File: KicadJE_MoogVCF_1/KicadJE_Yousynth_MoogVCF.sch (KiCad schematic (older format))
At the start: 44 parts

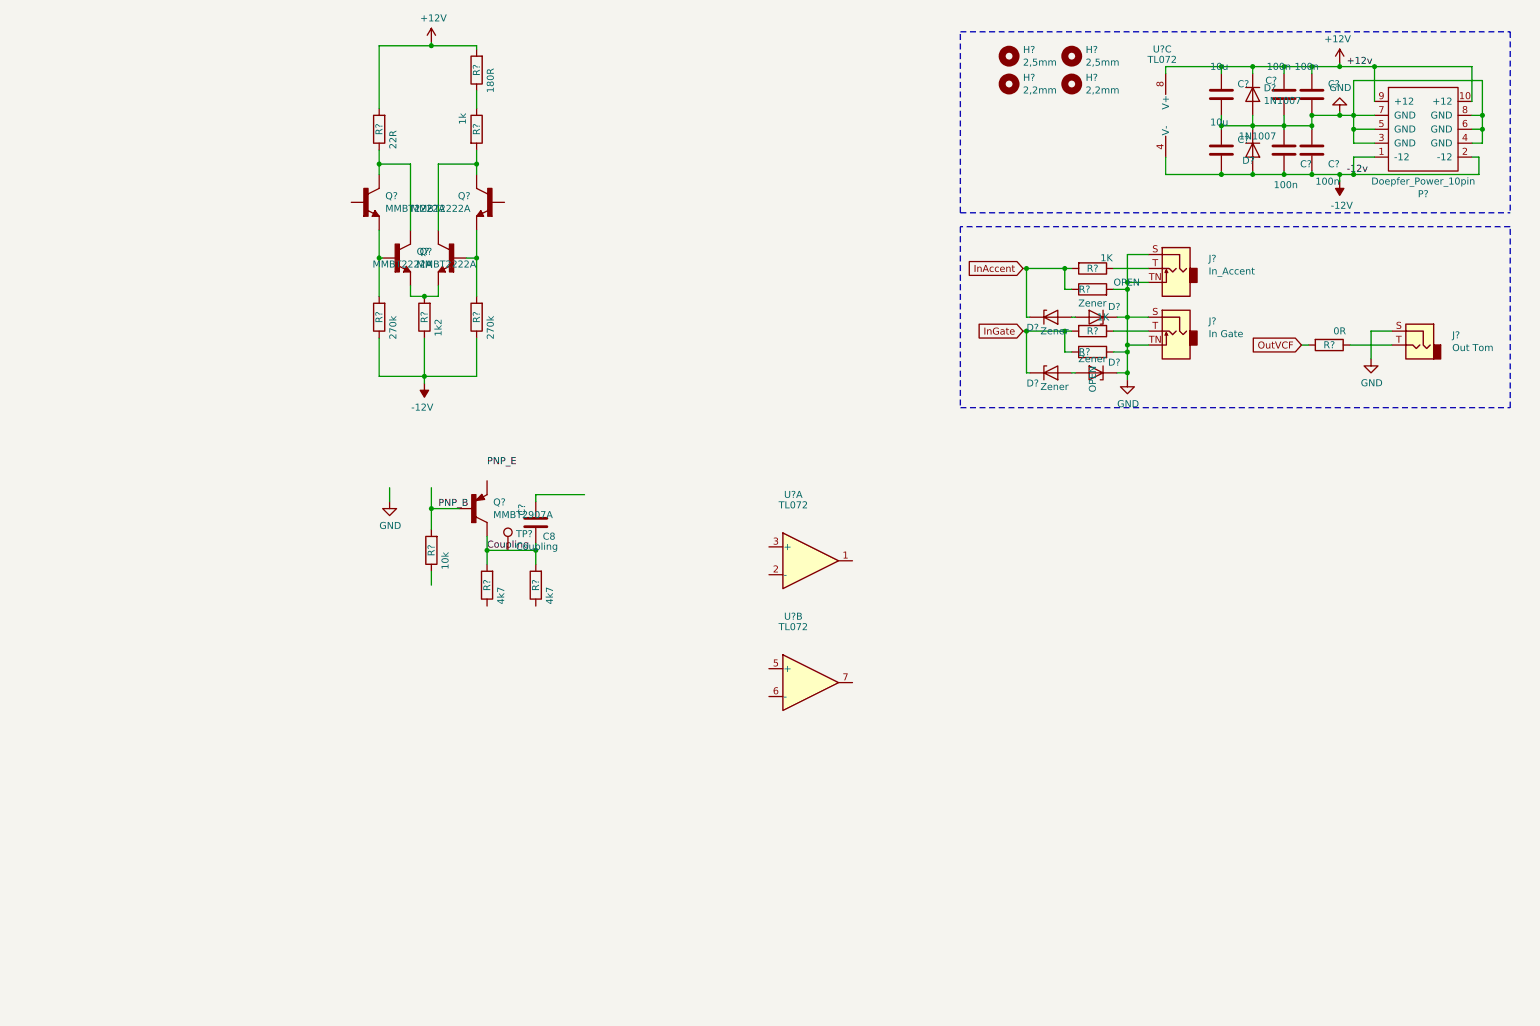
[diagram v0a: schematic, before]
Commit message: Moog Output stage
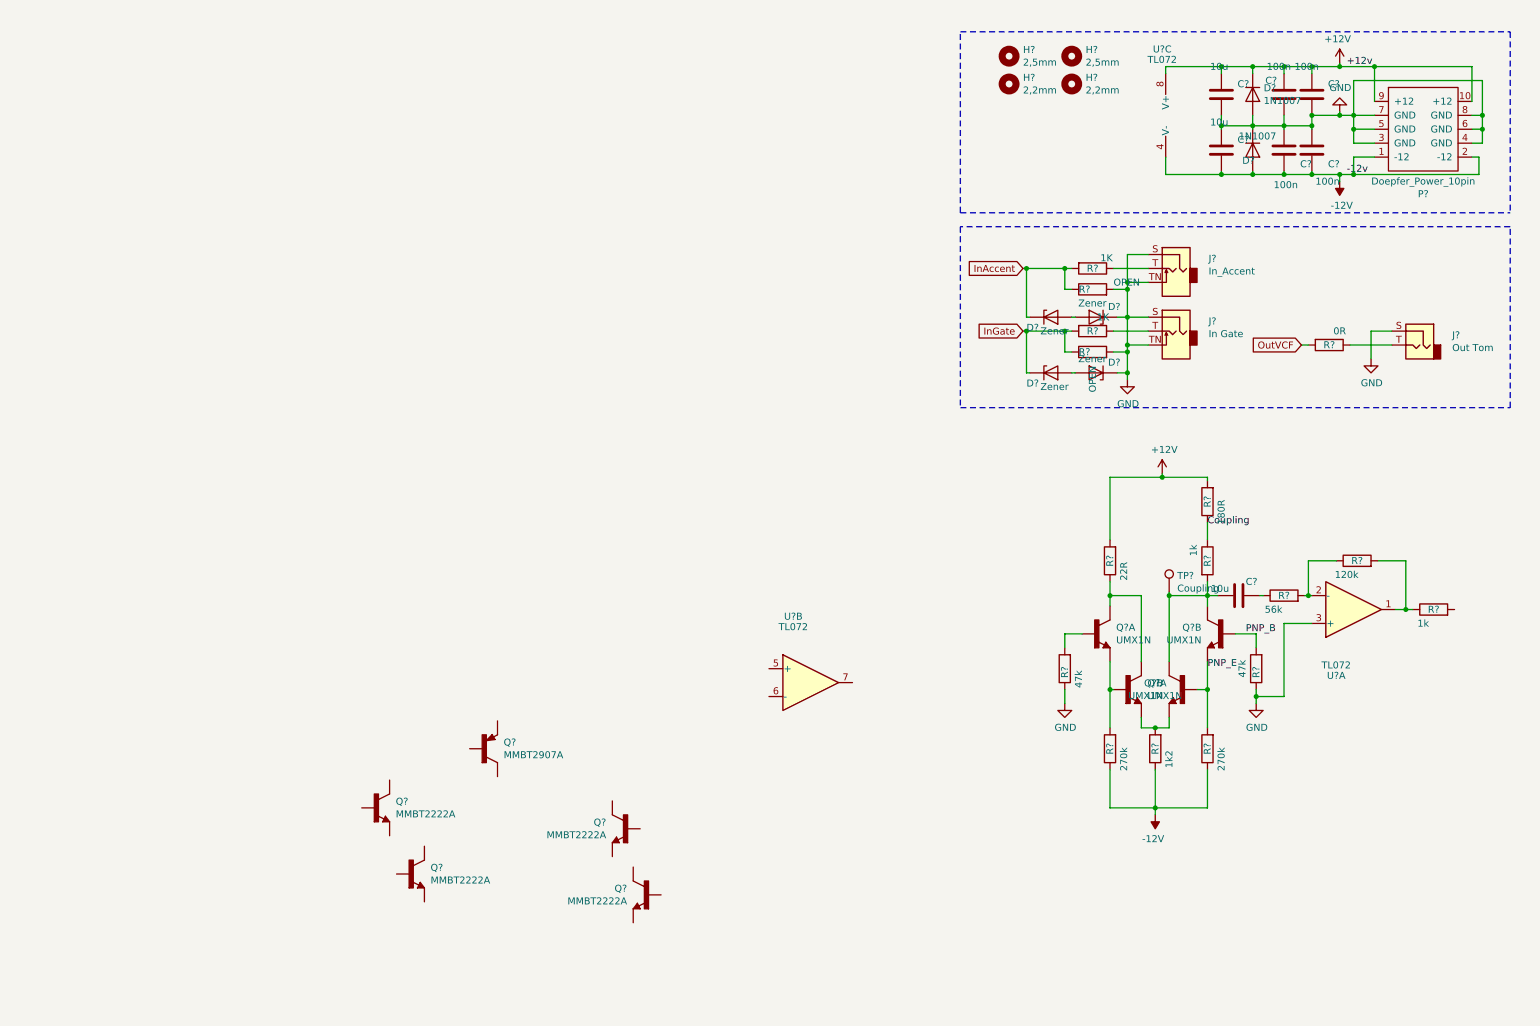
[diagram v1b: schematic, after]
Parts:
- added Q? (x4): UMX1N, UMT6, symbol UMX1N:UMX1N
- added R?: 47k, Resistor_SMD:R_0805_2012Metric_Pad1.15x1.40mm_HandSolder, symbol Device:R
- added R?: 120k, Resistor_SMD:R_0805_2012Metric_Pad1.15x1.40mm_HandSolder, symbol Device:R
- C?: value C8 -> 10u
- R?: value 10k -> 56k
- R?: value 4k7 -> 1k
- R?: value 4k7 -> 47k
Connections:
- wire segments 138 -> 147
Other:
- moved on the sheet: C?, Q?, R?, TP?, U?A

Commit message: Footprints
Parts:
- removed Q? (x3): MMBT2222A, Package_TO_SOT_SMD:SOT-23_Handsoldering, symbol MMBT2222A:MMBT2222A
- added C207, C208, C209, C210: 47n, Capacitor_SMD:C_0805_2012Metric_Pad1.15x1.40mm_HandSolder, symbol Device:C
- added C212: 10u, Capacitor_SMD:C_0805_2012Metric_Pad1.15x1.40mm_HandSolder, symbol Device:C
- added C213: Opt_220u, Capacitor_THT:CP_Radial_D10.0mm_P5.00mm, symbol Device:CP
- added C214: 22u, Capacitor_SMD:C_0805_2012Metric_Pad1.15x1.40mm_HandSolder, symbol Device:C
- added C215: 100p, Capacitor_SMD:C_0805_2012Metric_Pad1.15x1.40mm_HandSolder, symbol Device:C
- added D203, D204: Zener, Diode_SMD:D_MiniMELF, symbol Device:D_Zener
- added J201: CV2, AJ-Dropbox-Kicad:PJ301SM, symbol Connector:AudioJack2_SwitchT
- added Q201, Q208: UMX1N, AJ:UMX1N_UMT6_DualNPN, symbol UMX1N:UMX1N
- added Q202, Q203, Q204, Q205, Q207, Q211: SS9014, Package_TO_SOT_SMD:SOT-23_Handsoldering, symbol MMBT2222A:MMBT2222A
- added R201, R229: 330R, Resistor_SMD:R_0805_2012Metric_Pad1.15x1.40mm_HandSolder, symbol Device:R
- added R202: 1K, Resistor_SMD:R_0805_2012Metric_Pad1.15x1.40mm_HandSolder, symbol Device:R
- added R204: OPEN, Resistor_SMD:R_0805_2012Metric_Pad1.15x1.40mm_HandSolder, symbol Device:R
- added R206, R210, R213, R224: 150R, Resistor_SMD:R_0805_2012Metric_Pad1.15x1.40mm_HandSolder, symbol Device:R
- added R211: 0R, Resistor_SMD:R_0805_2012Metric_Pad1.15x1.40mm_HandSolder, symbol Device:R
- added R212: Open, Resistor_SMD:R_0805_2012Metric_Pad1.15x1.40mm_HandSolder, symbol Device:R
- added R218, R221: 120k, Resistor_SMD:R_0805_2012Metric_Pad1.15x1.40mm_HandSolder, symbol Device:R
- added R219: 56k, Resistor_SMD:R_0805_2012Metric_Pad1.15x1.40mm_HandSolder, symbol Device:R
- added R223: 10k, Resistor_SMD:R_0805_2012Metric_Pad1.15x1.40mm_HandSolder, symbol Device:R
- added R225, R239: 470R, Resistor_SMD:R_0805_2012Metric_Pad1.15x1.40mm_HandSolder, symbol Device:R
- added R228: 1k, Resistor_SMD:R_0805_2012Metric_Pad1.15x1.40mm_HandSolder, symbol Device:R
- added R233: 220R, Resistor_SMD:R_0805_2012Metric_Pad1.15x1.40mm_HandSolder, symbol Device:R
- added R234, R238: 100k, Resistor_SMD:R_0805_2012Metric_Pad1.15x1.40mm_HandSolder, symbol Device:R
- added R235: 680R, Resistor_SMD:R_0805_2012Metric_Pad1.15x1.40mm_HandSolder, symbol Device:R
- added R236: 150k, Resistor_SMD:R_0805_2012Metric_Pad1.15x1.40mm_HandSolder, symbol Device:R
- added R237: 1k8, Resistor_SMD:R_0805_2012Metric_Pad1.15x1.40mm_HandSolder, symbol Device:R
- added RV201: 50k_emphasis, AJ-Dropbox-Kicad:Potentiometer_China_RK09_Single_Vertical_AJ, symbol Envelope-cache-2018-08-04-13-00-04:POT
- added RV202: 1k, AJ-Dropbox-Kicad:Bourns3296WV, symbol Device:R_POT_TRIM
- added RV203: 50k_CV1, AJ-Dropbox-Kicad:Potentiometer_China_RK09_Single_Vertical_AJ, symbol Envelope-cache-2018-08-04-13-00-04:POT
- added RV204: 10k_Freq, AJ-Dropbox-Kicad:Potentiometer_China_RK09_Single_Vertical_AJ, symbol Envelope-cache-2018-08-04-13-00-04:POT
- added RV205: 500R, AJ-Dropbox-Kicad:Bourns3296WV, symbol Device:R_POT_TRIM
- added TP202: Input, TestPoint:TestPoint_Pad_1.5x1.5mm, symbol Connector:TestPoint
- J202: renamed from J?; value In_Accent -> Input
- J203: renamed from J?; value In Gate -> CV1
- J204: renamed from J?; value Out Tom -> Out VCF
- Q206: renamed from Q?; value MMBT2222A -> SS9014
- Q209, Q210: renamed from Q?; footprint UMT6 -> AJ:UMX1N_UMT6_DualNPN
- Q212: renamed from Q?; value MMBT2907A -> SS9015
- TP201: renamed from TP?; value Coupling -> PreOut
- gave numbers to parts that had none: 35
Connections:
- net +12V: now also Q201.2 (B), Q201.5 (B), R201.1, R201.2, R206.2, R235.2
- net Coupling: now also R212.1, RV201.3
- net GND: now also U201.5 (+), C213.2, C214.1, C215.1, D204.1 (K), J201.TN, Q211.2 (E), R204.2, R233.1, R239.1, RV203.3, RV204.3, RV205.2, RV205.3
- net OutVCF: now also R222.2
- net PNP_B: now also Q212.1 (B), C215.2, R234.2, R237.2, R238.2; no longer Q209.5 (B), R227.2
- net PNP_E: now also Q212.2 (E), Q211.1 (B); no longer Q209.4 (E), Q210.5 (B), R232.2
- net at Q212.3 (C): now also R239.2
- net at Q206.1 (B): now also Q207.1 (B), R213.1, R224.2
- net at Q206.2 (E): now also C210.2, Q208.6 (C)
- net at Q206.3 (C): now also C209.2, Q204.2 (E)
- net at U201.6 (-): now also R218.2, R219.1, R221.2
- net at U201.7: now also R219.2, R223.1
- net InAccent renamed InAudio
- net InAudio: now also R221.1
- net InGate renamed CV1
- net CV1: now also RV203.1
- new net: Q209.5 (B), R227.2
- new net: Q209.4 (E), Q210.5 (B), R232.2
- new net: J201.T, R202.1
- new net: D203.2 (A), D204.2 (A)
- new net: Q201.3 (C), Q201.6 (C)
- new net: C207.1, Q201.4 (E), Q203.3 (C)
- new net: C207.2, Q201.1 (E), Q202.3 (C)
- new net: C210.1, Q207.2 (E), Q208.3 (C)
- new net: Q208.1 (E), Q208.4 (E), R228.2
- new net: Q208.5 (B), RV202.2
- new net: C212.1, Q208.2 (B), R225.2, TP202.1
- new net: C209.1, Q205.2 (E), Q207.3 (C)
- new net: Q204.1 (B), Q205.1 (B), R210.1, R213.2
- new net: C208.2, Q202.2 (E), Q204.3 (C)
- new net: C208.1, Q203.2 (E), Q205.3 (C)
- new net: Q202.1 (B), Q203.1 (B), R206.1, R210.2
- new net: Q211.3 (C), R228.1
- new net: C213.1, C214.2, R224.1, R225.1, R229.1, R233.2
- new net: R229.2, RV202.3
- new net: R211.1, RV201.1, RV202.1
- new net: R211.2, R212.2, RV201.2
- new net: R237.1, RV205.1
- new net: C212.2, R223.2
- new net: R238.1, RV203.2
- new net: R235.1, RV204.1
- new net: R236.2, RV204.2
- new net CV2: D203.1 (K), R202.2, R204.1, R234.1
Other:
- moved on the sheet: Q206, Q212, U201B

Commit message: Placing components
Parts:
- added D209, D210: Zener, Diode_SMD:D_MiniMELF, symbol Device:D_Zener
- added D?: LED, LED_SMD:LED_0805_2012Metric, symbol Device:LED
- added J205: Input, AJ-Dropbox-Kicad:PJ301SM, symbol Connector:AudioJack2_SwitchT
- added R240: 1K, Resistor_SMD:R_0805_2012Metric_Pad1.15x1.40mm_HandSolder, symbol Device:R
- added R241: OPEN, Resistor_SMD:R_0805_2012Metric_Pad1.15x1.40mm_HandSolder, symbol Device:R
- added R?: 12K, Resistor_SMD:R_0805_2012Metric_Pad1.15x1.40mm_HandSolder, symbol Device:R
- added RV206: 50k_CV2, AJ-Dropbox-Kicad:Potentiometer_China_RK09_Single_Vertical_AJ, symbol Envelope-cache-2018-08-04-13-00-04:POT
- J202: footprint Connector_Audio:Jack_3.5mm_Ledino_KB3SPRS_Horizontal -> AJ-Dropbox-Kicad:PJ301SM
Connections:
- net -12V: now also R?.1
- net CV2: now also RV206.1; no longer R234.1
- net GND: now also J201.S, D210.1 (K), D?.2 (A), J205.TN, R241.2, RV206.3
- net InAudio: now also D209.1 (K), R240.2, R241.1; no longer R221.1
- net InAudio1: now reaches R218.1
- new net: R234.1, RV206.2
- new net: J205.T, R240.1
- new net: D209.2 (A), D210.2 (A)
- new net: D?.1 (K), R?.2
- new net InAudio2: R221.1
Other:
- moved on the sheet: C201, C202, C203, C204, C205, C206, C207, C208, C209, C210, C211, C212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

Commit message: fixing links
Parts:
- J202: value Input -> Input2
- J205: value Input -> Input1
- gave numbers to parts that had none: 2
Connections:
- net GND: now also J205.S
- net InAudio1: now also D209.1 (K), R240.2, R241.1
- net InAudio2: now also D205.1 (K), R203.2, R205.1
- removed net InAudio: D205.1 (K), D209.1 (K), R203.2, R205.1, R240.2, R241.1
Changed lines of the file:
@@
 AR Path="/5D99B7BA/5D9E663D" Ref="J202"  Part="1"
 F 0 "J202" H 8592 2896 50  0000 R CNN
-F 1 "Input" H 8592 2805 50  0000 R CNN
+F 1 "Input2" H 8592 2805 50  0000 R CNN
 F 2 "AJ-Dropbox-Kicad:PJ301SM" H 8825 2825 50  0001 C CNN
 F 3 "~" H 8825 2825 50  0001 C CNN
@@
 CV1
 Text GLabel 7725 2825 0    50   Input ~ 0
-InAudio
+InAudio2
 $Comp
 L Connector:AudioJack2_SwitchT J?
@@
 AR Path="/5D99B7BA/5E638137" Ref="J205"  Part="1"
 F 0 "J205" H 8592 2296 50  0000 R CNN
-F 1 "Input" H 8592 2205 50  0000 R CNN
+F 1 "Input1" H 8592 2205 50  0000 R CNN
 F 2 "AJ-Dropbox-Kicad:PJ301SM" H 8825 2225 50  0001 C CNN
 F 3 "~" H 8825 2225 50  0001 C CNN
@@
 	8375 2225 8625 2225
 Text GLabel 7725 2225 0    50   Input ~ 0
-InAudio
+InAudio1
 Wire Wire Line
 	8475 2375 8475 2575
@@
 $EndComp
 Wire Wire Line
-	8600 2025 8450 2025
+	8625 2125 8475 2125
 Wire Wire Line
 	8100 2575 8125 2575
@@
 P 8100 1575
 AR Path="/5D99B81E/5EC4F764" Ref="R?"  Part="1"
-AR Path="/5D99B7BA/5EC4F764" Ref="R?"  Part="1"
-F 0 "R?" V 8100 1575 50  0000 C CNN
+AR Path="/5D99B7BA/5EC4F764" Ref="R242"  Part="1"
+F 0 "R242" V 8100 1575 50  0000 C CNN
 F 1 "12K" V 8025 1675 50  0000 C CNN
 F 2 "Resistor_SMD:R_0805_2012Metric_Pad1.15x1.40mm_HandSolder" V 8030 1575 50  0001 C CNN
@@
 Connection ~ 8675 1575
 $Comp
-L Device:LED D?
+L Device:LED D211
 U 1 1 5EC8D67F
 P 7675 1575
-F 0 "D?" H 7668 1320 50  0000 C CNN
+F 0 "D211" H 7668 1320 50  0000 C CNN
 F 1 "LED" H 7668 1411 50  0000 C CNN
 F 2 "LED_SMD:LED_0805_2012Metric" H 7675 1575 50  0001 C CNN
@@
 P 7500 1600
 AR Path="/5D99B81E/5ECCC823" Ref="#PWR?"  Part="1"
-AR Path="/5D99B7BA/5ECCC823" Ref="#PWR?"  Part="1"
-F 0 "#PWR?" H 7500 1350 50  0001 C CNN
+AR Path="/5D99B7BA/5ECCC823" Ref="#PWR0215"  Part="1"
+F 0 "#PWR0215" H 7500 1350 50  0001 C CNN
 F 1 "GND" H 7505 1427 50  0000 C CNN
 F 2 "" H 7500 1600 50  0001 C CNN

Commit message: all components placed
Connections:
- net +12V: now also Q201.3 (C), Q201.6 (C); no longer Q201.2 (B), Q201.5 (B), R201.1, R206.2
- net PNP_B: now also R236.1
- new net: Q201.2 (B), Q201.5 (B), R201.1, R206.2
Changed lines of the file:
@@
 $EndComp
-Wire Wire Line
-	3250 1275 3750 1275
 Wire Wire Line
 	3250 1275 3250 1575
@@
 	3475 1375 3475 1325
 Wire Wire Line
-	3475 1325 3975 1325
+	3475 1325 3750 1325
 Wire Wire Line
 	3975 1325 3975 1375
@@
 	1    0    0    -1
 $EndComp
-Connection ~ 3750 1275
-Wire Wire Line
-	3750 1275 4250 1275
 Wire Wire Line
 	3750 900  3750 950
@@
 Wire Wire Line
 	2900 3700 3250 3700
-Connection ~ 3750 950
-Wire Wire Line
-	3750 950  3750 1275
 Connection ~ 3250 3700
 Wire Wire Line
@@
 Connection ~ 2750 6550
 Wire Wire Line
-	2750 6550 3525 6550
+	2750 6550 3150 6550
 Wire Wire Line
 	3000 6975 3150 6975
@@
 Wire Wire Line
 	7525 1575 7500 1575
+Wire Wire Line
+	3250 1275 4250 1275
+Wire Wire Line
+	3750 950  3750 1325
+Connection ~ 3750 950
+Connection ~ 3750 1325
+Wire Wire Line
+	3750 1325 3975 1325
+Wire Wire Line
+	3150 6575 3150 6550
+Connection ~ 3150 6550
+Wire Wire Line
+	3150 6550 3525 6550
 $EndSCHEMATC
